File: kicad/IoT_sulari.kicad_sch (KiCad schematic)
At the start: 1 part, among them U1 nRF52840

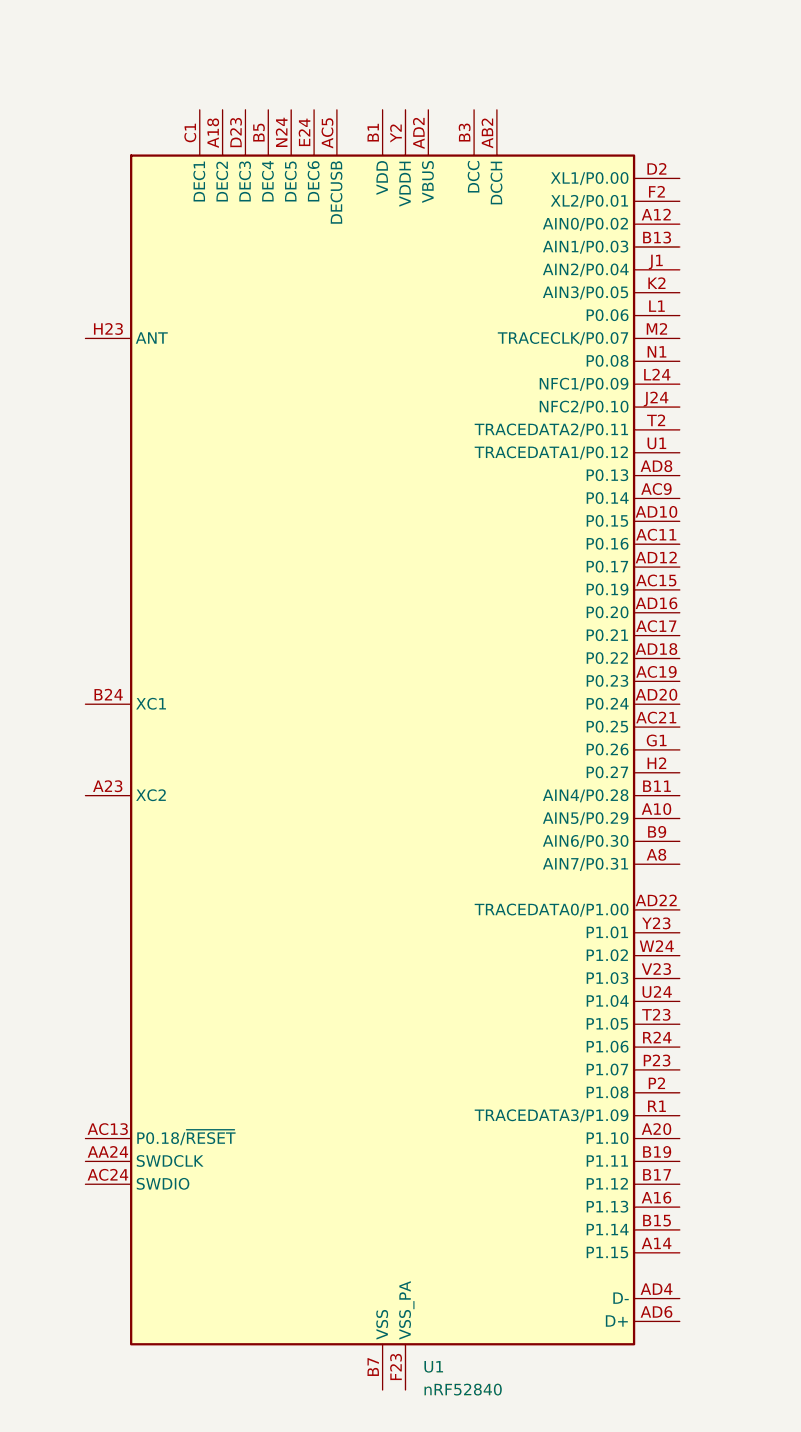
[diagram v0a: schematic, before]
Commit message: Add nRF9160 to KiCad project
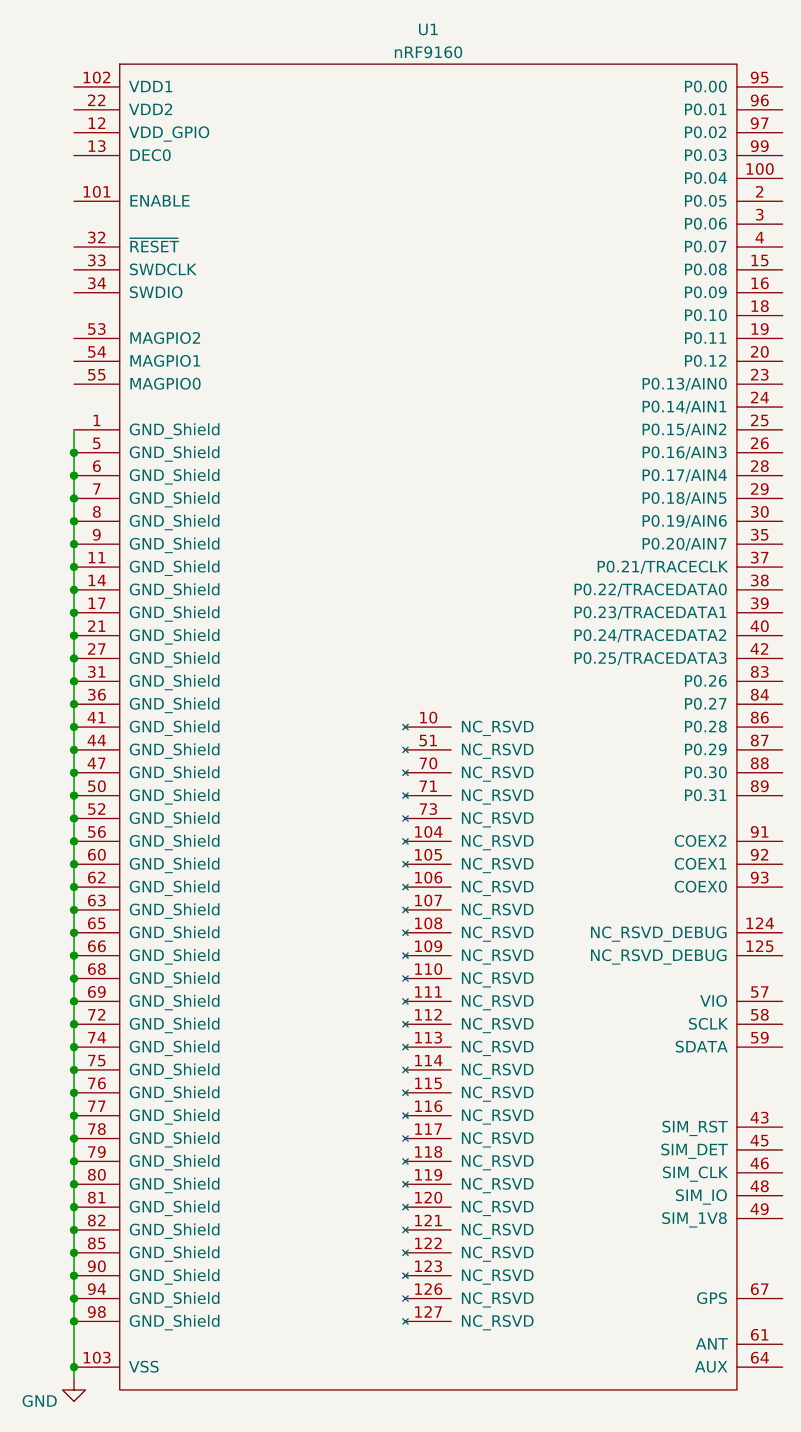
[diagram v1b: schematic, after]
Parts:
- removed U1: nRF52840, Package_DFN_QFN:Nordic_AQFN-73-1EP_7x7mm_P0.5mm, symbol MCU_Nordic:nRF52840
- added U1: nRF9160, symbol nrf9160:nRF9160
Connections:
- new net GND: U1.1 (GND_Shield), U1.103 (VSS), U1.11 (GND_Shield), U1.14 (GND_Shield), U1.17 (GND_Shield), U1.21 (GND_Shield), U1.27 (GND_Shield), U1.31 (GND_Shield), U1.36 (GND_Shield), U1.41 (GND_Shield), U1.44 (GND_Shield), U1.47 (GND_Shield), U1.5 (GND_Shield), U1.50 (GND_Shield), U1.52 (GND_Shield), U1.56 (GND_Shield), U1.6 (GND_Shield), U1.60 (GND_Shield), U1.62 (GND_Shield), U1.63 (GND_Shield), U1.65 (GND_Shield), U1.66 (GND_Shield), U1.68 (GND_Shield), U1.69 (GND_Shield), U1.7 (GND_Shield), U1.72 (GND_Shield), U1.74 (GND_Shield), U1.75 (GND_Shield), U1.76 (GND_Shield), U1.77 (GND_Shield), U1.78 (GND_Shield), U1.79 (GND_Shield), U1.8 (GND_Shield), U1.80 (GND_Shield), U1.81 (GND_Shield), U1.82 (GND_Shield), U1.85 (GND_Shield), U1.9 (GND_Shield), U1.90 (GND_Shield), U1.94 (GND_Shield), U1.98 (GND_Shield)

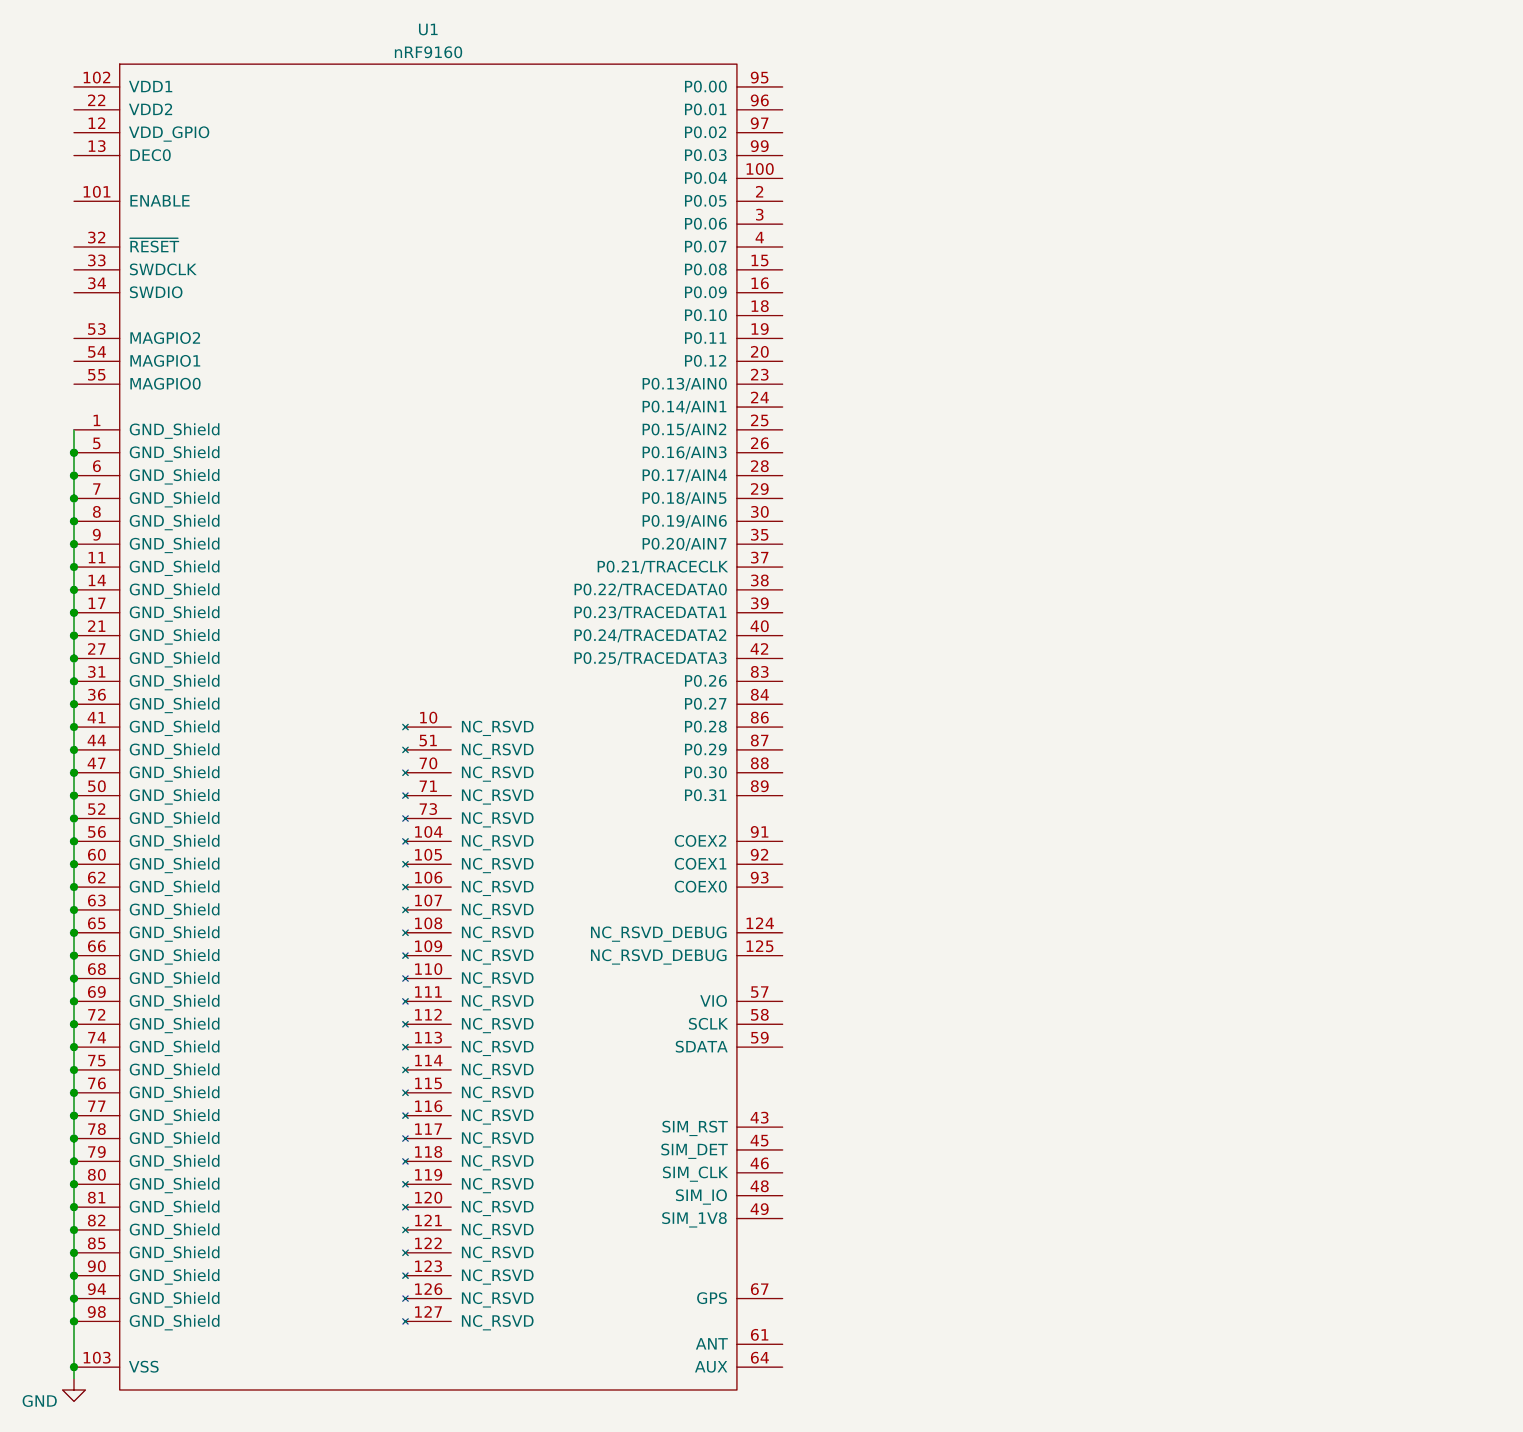
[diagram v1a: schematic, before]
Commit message: added TCR2EF33 symbol to kicad
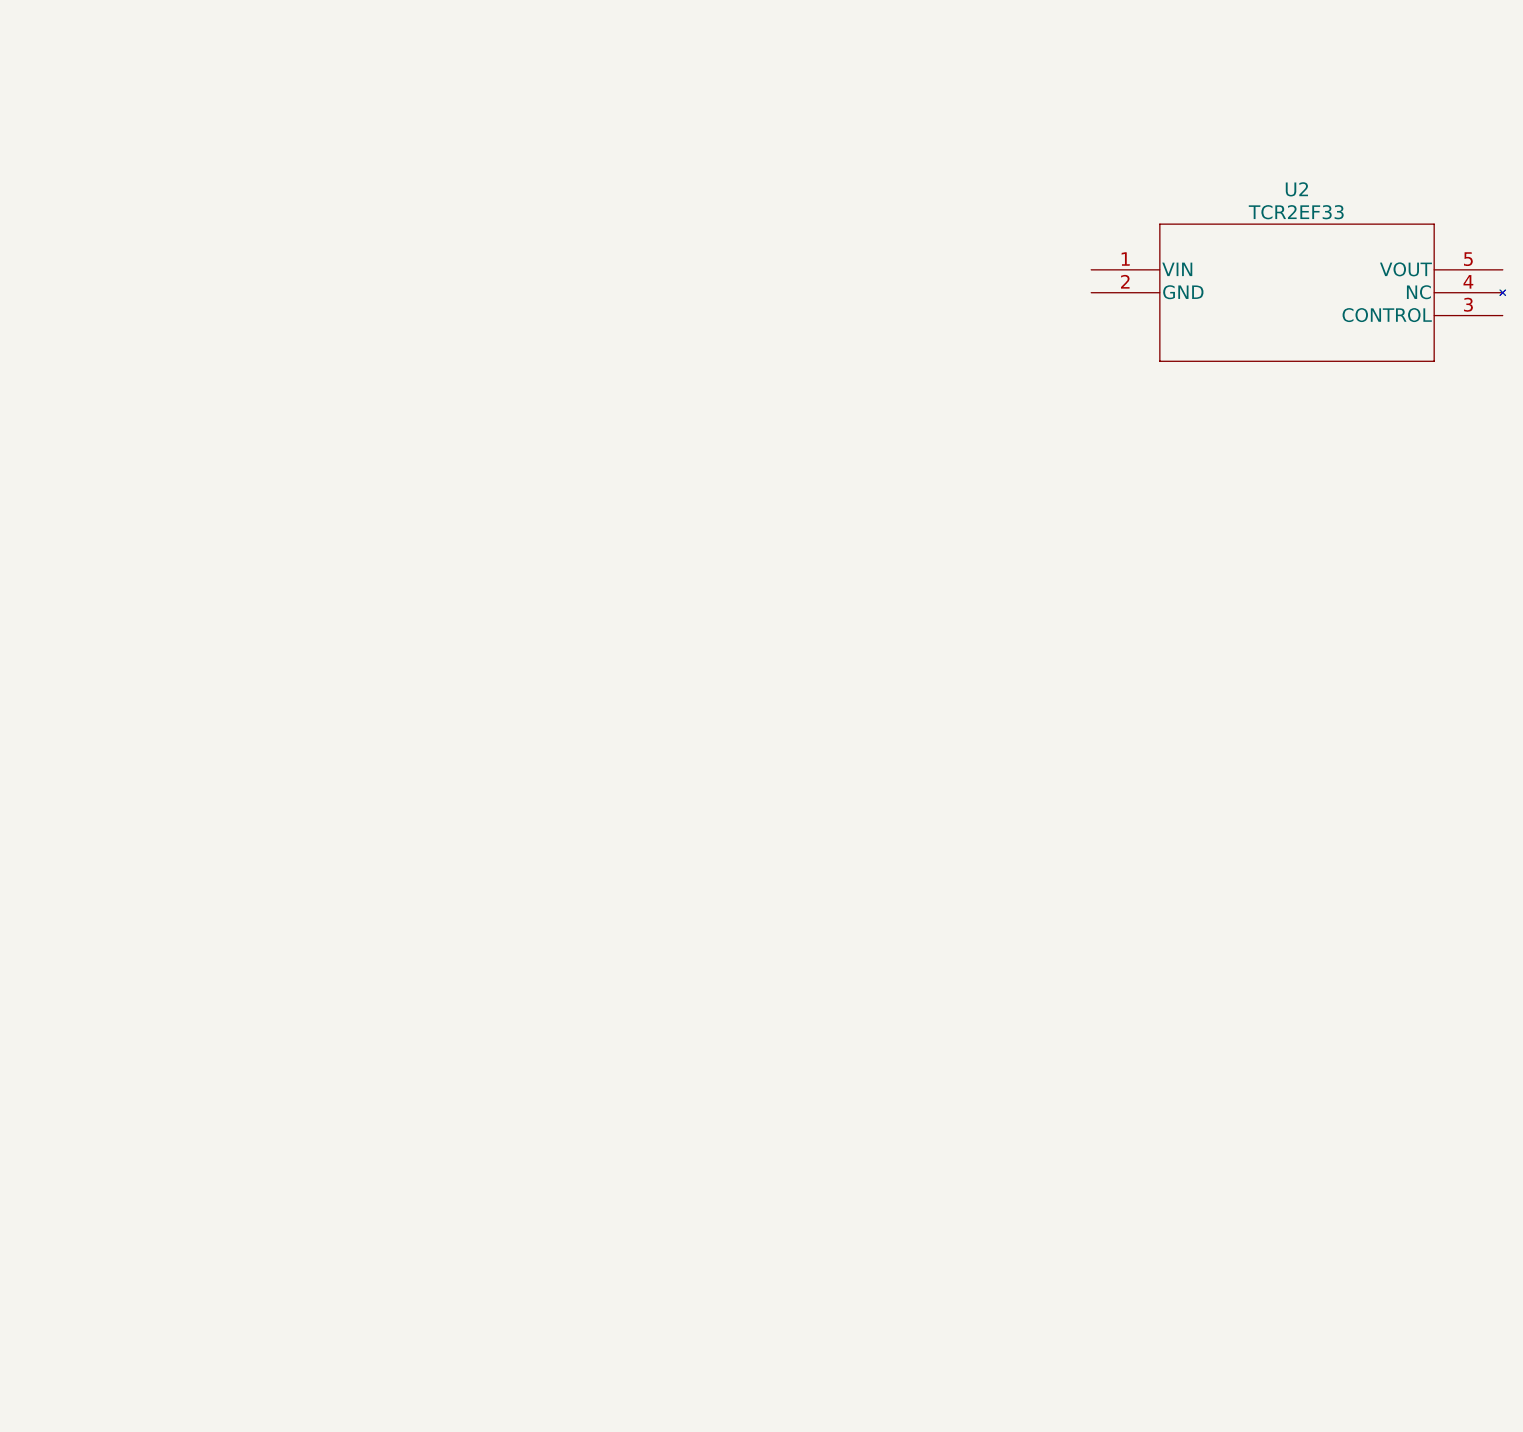
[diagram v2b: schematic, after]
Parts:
- removed U1: nRF9160, symbol nrf9160:nRF9160
- added U2: TCR2EF33, SOT-25 SMV_TOS, symbol TCR2EF33:TCR2EF33

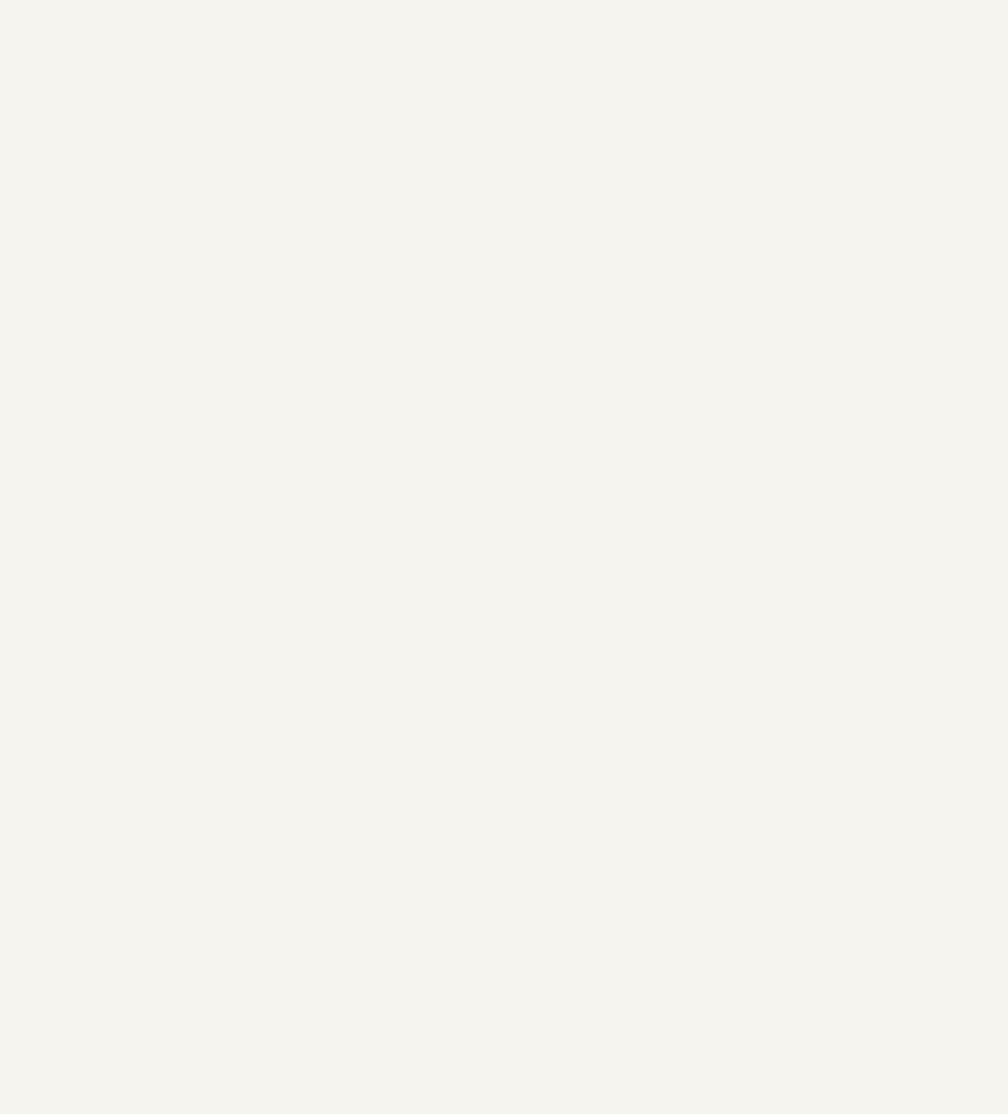
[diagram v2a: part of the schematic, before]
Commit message: Added NRF9160 symbol and footprint
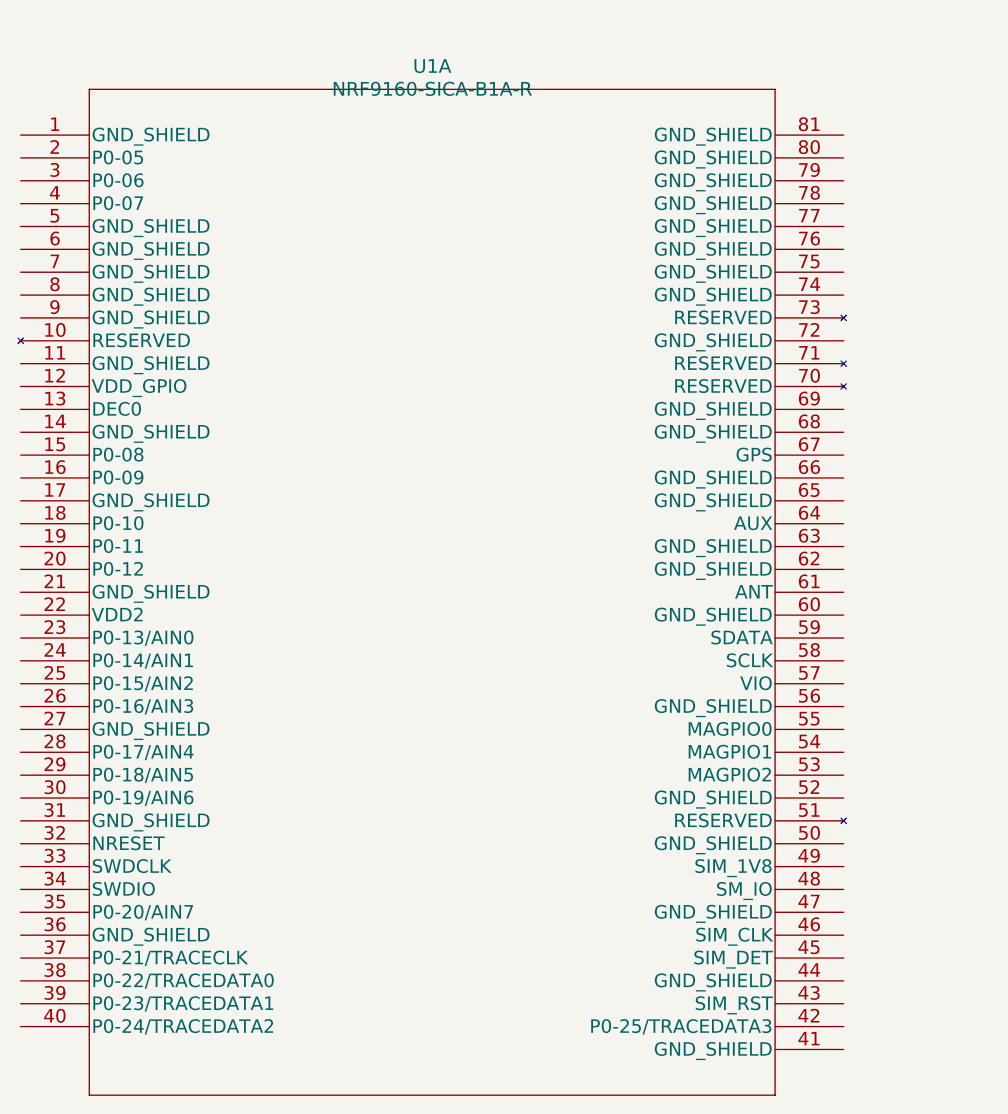
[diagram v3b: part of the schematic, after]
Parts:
- added U1: NRF9160-SICA-B1A-R, LGA_16X10P5_NOR, symbol NRF-9160-SICA-B1A-R:NRF9160-SICA-B1A-R
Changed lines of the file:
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@@
+    )
+  )
+  (symbol (lib_id "NRF-9160-SICA-B1A-R:NRF9160-SICA-B1A-R") (at 62.23 43.18 0) (unit 1)
+    (in_bom yes) (on_board yes) (dnp no) (fields_autoplaced)
+    (property "Reference" "U1" (at 107.95 35.56 0)
+      (effects (font (size 1.524 1.524)))
+    )
+    (property "Value" "NRF9160-SICA-B1A-R" (at 107.95 38.1 0)
+      (effects (font (size 1.524 1.524)))
+    )
+    (property "Footprint" "LGA_16X10P5_NOR" (at 107.95 37.084 0)
+      (effects (font (size 1.524 1.524)) hide)
+    )
+    (property "Datasheet" "" (at 62.23 43.18 0)
+      (effects (font (size 1.524 1.524)))
+    )
+    (pin "1")
+    (pin "10")
+    (pin "11")
+    (pin "12")
+    (pin "13")
+    (pin "14")
+    (pin "15")
+    (pin "16")
+    (pin "17")
+    (pin "18")
+    (pin "19")
+    (pin "2")
+    (pin "20")
+    (pin "21")
+    (pin "22")
+    (pin "23")
+    (pin "24")
+    (pin "25")
+    (pin "26")
+    (pin "27")
+    (pin "28")
+    (pin "29")
+    (pin "3")
+    (pin "30")
+    (pin "31")
+    (pin "32")
+    (pin "33")
+    (pin "34")
+    (pin "35")
+    (pin "36")
+    (pin "37")
+    (pin "38")
+    (pin "39")
+    (pin "4")
+    (pin "40")
+    (pin "41")
+    (pin "42")
+    (pin "43")
+    (pin "44")
+    (pin "45")
+    (pin "46")
+    (pin "47")
+    (pin "48")
+    (pin "49")
+    (pin "5")
+    (pin "50")
+    (pin "51")
+    (pin "52")
+    (pin "53")
+    (pin "54")
+    (pin "55")
+    (pin "56")
+    (pin "57")
+    (pin "58")
+    (pin "59")
+    (pin "6")
+    (pin "60")
+    (pin "61")
+    (pin "62")
+    (pin "63")
+    (pin "64")
+    (pin "65")
+    (pin "66")
+    (pin "67")
+    (pin "68")
+    (pin "69")
+    (pin "7")
+    (pin "70")
+    (pin "71")
+    (pin "72")
+    (pin "73")
+    (pin "74")
+    (pin "75")
+    (pin "76")
+    (pin "77")
+    (pin "78")
+    (pin "79")
+    (pin "8")
+    (pin "80")
+    (pin "81")
+    (pin "9")
+    (pin "100")
+    (pin "101")
+    (pin "102")
+    (pin "103")
+    (pin "104")
+    (pin "105")
+    (pin "106")
+    (pin "107")
+    (pin "108")
+    (pin "109")
+    (pin "110")
+    (pin "111")
+    (pin "112")
+    (pin "113")
+    (pin "114")
+    (pin "115")
+    (pin "116")
+    (pin "117")
+    (pin "118")
+    (pin "119")
+    (pin "120")
+    (pin "121")
+    (pin "122")
+    (pin "123")
+    (pin "124")
+    (pin "125")
+    (pin "126")
+    (pin "127")
+    (pin "128")
+    (pin "129")
+    (pin "130")
+    (pin "131")
+    (pin "132")
+    (pin "133")
+    (pin "134")
+    (pin "135")
+    (pin "136")
+    (pin "137")
+    (pin "138")
+    (pin "139")
+    (pin "140")
+    (pin "141")
+    (pin "142")
+    (pin "143")
+    (pin "144")
+    (pin "145")
+    (pin "146")
+    (pin "147")
+    (pin "148")
+    (pin "149")
+    (pin "150")
+    (pin "151")
+    (pin "152")
+    (pin "153")
+    (pin "154")
+    (pin "155")
+    (pin "156")
+    (pin "157")
+    (pin "158")
+    (pin "159")
+    (pin "160")
+    (pin "161")
+    (pin "82")
+    (pin "83")
+    (pin "84")
+    (pin "85")
+    (pin "86")
+    (pin "87")
+    (pin "88")
+    (pin "89")
+    (pin "90")
+    (pin "91")
+    (pin "92")
+    (pin "93")
+    (pin "94")
+    (pin "95")
+    (pin "96")
+    (pin "97")
+    (pin "98")
+    (pin "99")
+    (instances
+      (project "IoT_sulari"
+        (path "/184b47ed-2c2b-4c02-be35-d18f4f4e5685"
+          (reference "U1") (unit 1)
+        )
+      )
     )
   )
